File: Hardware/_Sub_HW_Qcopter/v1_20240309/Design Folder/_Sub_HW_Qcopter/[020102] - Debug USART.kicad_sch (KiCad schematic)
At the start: 3 parts, among them J701 HDR_1X3_THD-1.27MM

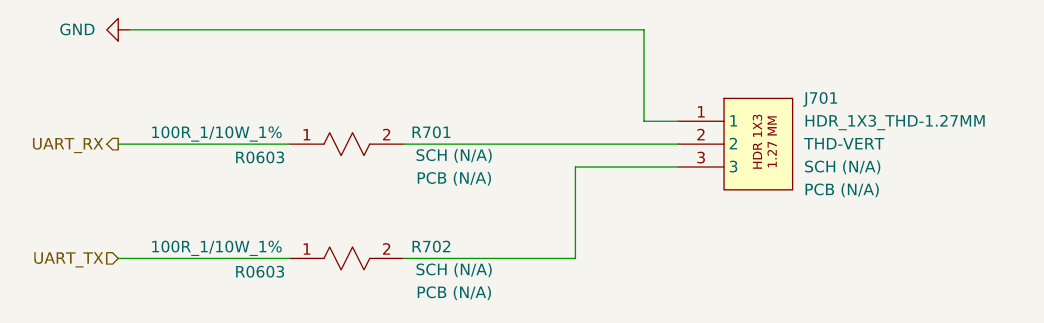
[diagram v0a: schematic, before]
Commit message: Update [020102] - Debug USART.kicad_sch
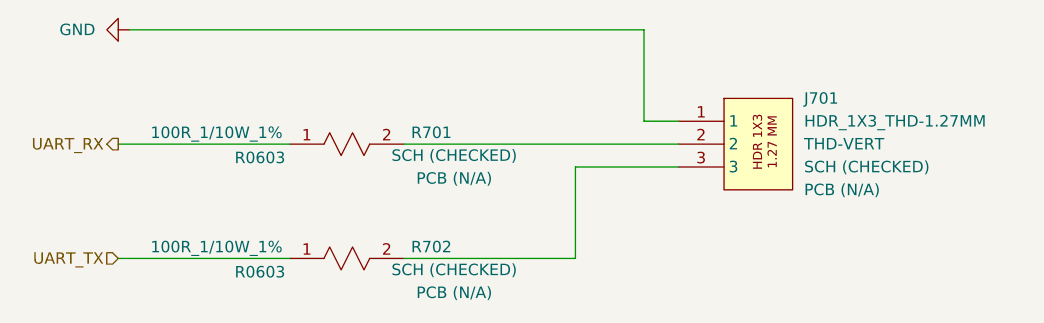
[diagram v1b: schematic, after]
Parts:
- J701, R701, R702: SCH CHECK SCH (N/A) -> SCH (CHECKED)
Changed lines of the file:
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@@
 			)
 		)
-		(property "SCH CHECK" "SCH (N/A)"
+		(property "SCH CHECK" "SCH (CHECKED)"
 			(at 279.4 205.7399 0)
 			(effects
@@
 			)
 		)
-		(property "SCH CHECK" "SCH (N/A)"
+		(property "SCH CHECK" "SCH (CHECKED)"
 			(at 240.538 204.47 0)
 			(effects
@@
 			)
 		)
-		(property "SCH CHECK" "SCH (N/A)"
+		(property "SCH CHECK" "SCH (CHECKED)"
 			(at 240.538 217.17 0)
 			(effects
